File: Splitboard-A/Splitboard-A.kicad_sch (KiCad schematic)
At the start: 111 parts, among them J1 USB_C_Receptacle_USB2.0, J2 USB_C_Receptacle, J3 Conn_01x07, K1 KEYSW, K10 KEYSW, K11 KEYSW, K12 KEYSW, K13 KEYSW, K14 KEYSW, K15 KEYSW, K16 KEYSW, K17 KEYSW, K18 KEYSW, K19 KEYSW, K2 KEYSW, K20 KEYSW, K21 KEYSW, K22 KEYSW, K23 KEYSW, K24 KEYSW, K25 KEYSW, K26 KEYSW, K27 KEYSW, K28 KEYSW, K29 KEYSW, K3 KEYSW, K30 KEYSW, K31 KEYSW, K32 KEYSW, K33 KEYSW, K34 KEYSW, K35 KEYSW, K36 KEYSW, K37 KEYSW, K38 KEYSW, K4 KEYSW, K5 KEYSW, K6 KEYSW, K7 KEYSW, K8 KEYSW, K9 KEYSW, SW1 RotaryEncoder, SW2 SW_Push, U1 AMS1117-3.3, U2 STM32F407VGTx, U3 CR2013-MI2120

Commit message: updated some pins and net labels on sba
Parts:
- C4: value 100nF -> (none)
- C5: value 100nF -> 1uf
- J3: value Conn_01x07 -> (none)
- SW2: value SW_Push -> (none)
- renumbered C1 to C3, C3 to C4, D4 to D1, D13 to D10, D14 to D11, D15 to D12, D16 to D13, D17 to D14, D18 to D15, D19 to D16, D20 to D17, D21 to D18, D22 to D19, D5 to D2, D23 to D20, D24 to D21, D25 to D22, D26 to D23, D27 to D24, D28 to D25, D29 to D26, D30 to D27, D31 to D28, D32 to D29, D6 to D3, D33 to D30, D34 to D31, D35 to D32, D36 to D33, D37 to D34, D38 to D35, D39 to D36, D40 to D37, D41 to D38, D1 to D39, D7 to D4, D2 to D40, D3 to D41, D8 to D5, D9 to D6, D10 to D7, D11 to D8, D12 to D9, J2 to J1, J1 to J2, R3 to R1, R4 to R2, R1 to R3, R2 to R4, U2 to U1, U1 to U2
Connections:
- net +3v3 to micro is gone; now on net +3.3V: C4.1, R3.2, R4.2, U2.2 (VO)
- net Power Regulator is gone; now on net +3.3V: C3.1, D40.2 (A), D41.1 (K), R4.1
- net LCD1_DC: now reaches U1.64 (PC7)
- net LCD1_CS: now reaches U1.65 (PC8)
- net LCD2_DC: now reaches U1.66 (PC9)
- net LCD2_CS: now reaches U1.67 (PA8)
- net LCD2_RESET: now reaches U1.68 (PA9)
- net LCD1_RESET: now reaches U1.69 (PA10)
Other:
- moved on the sheet: U1

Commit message: Updated Schematics with suggestions from course staff
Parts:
- removed C3: 0.1uF, Resistor_SMD:R_0805_2012Metric, symbol Device:C
- removed D40, D41: D_Schottky, Diode_SMD:D_SOD-123, symbol Device:D_Schottky
- removed F1: 500mA, Fuse:Fuse_BelFuse_0ZRE0125FF_L21.2mm_W5.3mm, symbol Device:Fuse
- removed J3: (no value), symbol Connector_Generic:Conn_01x07
- removed R3: 10K, Resistor_SMD:R_0805_2012Metric, symbol Device:R
- added C1, C2: 2u2, Capacitor_SMD:C_0805_2012Metric, symbol Device:C
- added C16, C17: .01uF, Capacitor_SMD:C_0805_2012Metric, symbol Device:C
- added C5, C? (x2): 100nF, Capacitor_SMD:C_0805_2012Metric, symbol Device:C
- added C?: 10uf, Capacitor_SMD:C_0805_2012Metric, symbol Device:C
- added D? (x2): D_Schottky, Diode_SMD:D_SOD-123, symbol Device:D_Schottky
- added J3: Conn_01x06, Connector_PinHeader_2.54mm:PinHeader_1x06_P2.54mm_Horizontal, symbol Connector_Generic:Conn_01x06
- added R10, R11, R12, R13, R14, R5, R6, R7, R8, R9: 10k, Resistor_SMD:R_0805_2012Metric, symbol Device:R
- added R15: 10K, Resistor_SMD:R_0805_2012Metric, symbol Device:R
- added R? (x23): 20, Resistor_SMD:R_0805_2012Metric, symbol Device:R
- added R? (x2): 4k7, Resistor_SMD:R_0805_2012Metric, symbol Device:R
- added U1: SIT2024BA-S2-33E-8.000000G, SIT2024BA:SIT2024BA-S2-33E-8.000000G, symbol SIT2024BA:SIT2024BA-S2-33E-8.000000G
- added U5: USBUF02W6, ul_USBUF02W6:USBUF02W6, symbol USBUF02W6:USBUF02W6
- C10: renamed from C9; footprint (none) -> Capacitor_SMD:C_0805_2012Metric
- C11: renamed from C10; footprint (none) -> Capacitor_SMD:C_0805_2012Metric
- C12: renamed from C11; footprint (none) -> Capacitor_SMD:C_0805_2012Metric
- C13: renamed from C12; footprint (none) -> Capacitor_SMD:C_0805_2012Metric
- C14: renamed from C13; footprint (none) -> Capacitor_SMD:C_0805_2012Metric
- C15: renamed from C14; footprint (none) -> Capacitor_SMD:C_0805_2012Metric
- C18: renamed from C4; value (none) -> 100nF; footprint (none) -> Capacitor_SMD:C_0805_2012Metric
- C6: renamed from C5; value 1uf -> 10uf; footprint (none) -> Capacitor_SMD:C_0805_2012Metric
- C7: renamed from C6; footprint (none) -> Capacitor_SMD:C_0805_2012Metric
- C8: renamed from C7; footprint (none) -> Capacitor_SMD:C_0805_2012Metric
- C9: renamed from C8; footprint (none) -> Capacitor_SMD:C_0805_2012Metric
- J1: renamed from J2; footprint USB_C_Receptacle_GCT_USB4085 -> Connector_USB:USB_C_Receptacle_Amphenol_12401548E4-2A
- J2: renamed from J1; footprint USB_C_Receptacle_GCT_USB4085 -> Connector_USB:USB_C_Receptacle_Amphenol_12401548E4-2A
- R1, R2: value R -> 5K1; footprint (none) -> Resistor_SMD:R_0805_2012Metric
- R4: value 100K -> 10k
- SW1: footprint Rotary_Encoder:RotaryEncoder_Alps_EC12E_Vertical_H20mm -> Rotary_Encoder:RotaryEncoder_Alps_EC11E-Switch_Vertical_H20mm
- SW2: value (none) -> SW_Push; footprint (none) -> Button_Switch_THT:SW_PUSH_6mm
- renumbered C2 to C3, U3 to U2, U1 to U3, U2 to U4
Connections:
- net LCD1_RESET is gone; now on net LCD1_RST: U3.69 (PA10)
- net +3.3V: now also U2.8 (LED), U3.21 (VREF+), U3.22 (VDDA), U3.6 (VBAT), C?.1, D?.1 (K), D?.1 (K), R10.2, R11.1, R13.1, R15.1, R5.2, R6.2, R7.2, R8.2, R9.2, R?.2, R?.2, U1.3 (OE/NC), U1.4 (VDD), U5.5 (VDD); no longer C4.1, J2.A4 (VBUS), J2.A9 (VBUS), J2.B4 (VBUS), J2.B9 (VBUS), R1.1, R2.1, R4.1, U2.1 (VCC), U4.2 (VO)
- net ENC_A: now also C16.1, R12.1, R?.2; no longer R1.2, SW1.A, U3.60 (PD13)
- net ENC_B: now also C17.2, R14.2, R?.2; no longer R2.2, SW1.B, U3.61 (PD14)
- net GND: now also R1.2, R2.2, SW1.S2, U3.20 (VSSA), U3.94 (BOOT0), C1.2, C16.2, C17.1, C2.2, C5.1, C?.2, C?.2, C?.2, J3.3 (Pin_3), U1.1 (GND), U5.2 (GND)
- net LCD1_CS: now also U2.3 (~{CS})
- net LCD1_DC: now also U2.5 (D/~{C})
- net LCD2_CS: now also R?.1
- net LCD2_DC: now also R?.1
- net MOSI: now also U3.18 (PC3), R?.1; no longer J2.B11 (RX1+)
- net NRST: now also J3.5 (Pin_5), R15.2
- net SCK: now also U3.52 (PB13), R?.1; no longer J2.A2 (TX1+)
- net SCL: now also R?.1, R?.1; no longer J2.A10 (RX2-)
- net SDA: now also R?.1, R?.1; no longer J2.A11 (RX2+)
- net SWCLK: now also J3.2 (Pin_2)
- net SWDIO: now also J3.4 (Pin_4)
- net SWO: now also J3.6 (Pin_6)
- net col0: now also R9.1, R?.2; no longer U3.88 (PD7)
- net col1: now also R8.1, R?.2; no longer U3.55 (PD8)
- net col2: now also R7.1, R?.2; no longer U3.56 (PD9)
- net col3: now also R6.1, R?.2; no longer U3.57 (PD10)
- net col4: now also R5.1, R?.2; no longer U3.58 (PD11)
- net col5: now also R4.1, R?.2; no longer U3.59 (PD12)
- net row0: now also R?.2; no longer U3.81 (PD0)
- net row1: now also R?.2; no longer U3.82 (PD1)
- net row2: now also R?.2; no longer U3.83 (PD2)
- net row3: now also R?.2; no longer U3.84 (PD3)
- net row4: now also R?.2; no longer U3.85 (PD4)
- net row5: now also R?.2; no longer U3.86 (PD5)
- net row6: now also R?.2; no longer U3.87 (PD6)
- net at J1.A5 (CC1): now also R1.1
- net at J1.B5 (CC2): now also R2.1
- net USB_CONN_D+: now reaches J1.B6 (D+)
- net USB_CONN_D+: now also J1.A6 (D+), U5.1 (D1)
- net USB_CONN_D-: now reaches J1.B7 (D-)
- net USB_CONN_D-: now also J1.A7 (D-), U5.3 (D2)
- net ENC_SW: now reaches SW1.S1
- net ENC_SW: now also C5.2, R10.1, R?.2
- net at D39.1 (K): now also FB1.1
- net RCC_OSC_IN: now reaches U3.12 (PH0)
- net RCC_OSC_IN: now also U1.5 (OUT)
- net RCC_OSC_OUT: now reaches U3.13 (PH1)
- net at U3.49 (VCAP_1): now also C1.1
- net at U3.62 (PD15): now also R?.1
- net at U3.73 (VCAP_2): now also C2.1
- net LCD1_RST: now reaches U2.4 (RESET)
- net at J2.A5 (CC1): now also J2.B5 (CC2), R?.2
- net at J2.A6 (D+): now also J2.B6 (D+), R?.2
- net at J2.A7 (D-): now also J2.B7 (D-), R?.2
- net at J2.A8 (SBU1): now also J2.B8 (SBU2), R?.2
- net at J2.B2 (TX2+): now also J2.A2 (TX1+)
- net at J2.B3 (TX2-): now also J2.A3 (TX1-), R?.2
- net CS: no longer names the net of J2.B10 (RX1-)
- net CS: now also J2.A10 (RX2-), R?.2; no longer U2.3 (~{CS})
- net LCD2_RESET renamed LCD2_RST
- net LCD2_RST: now also R?.1
- net MISO: no longer names the net of U2.9 (MISO)
- net MISO: no longer J2.A3 (TX1-)
- net TRST: no longer names the net of U3.90 (PB4)
- net USB_DM renamed USB_D-
- net USB_D-: now also U5.4 (D3); no longer J1.A7 (D-)
- net USB_DP renamed USB_D+
- net USB_D+: now also U5.6 (D4); no longer J1.A6 (D+)
- net Voltage Regulator Input renamed VBUS
- net VBUS: now also J2.A4 (VBUS), J2.A9 (VBUS), J2.B4 (VBUS), J2.B9 (VBUS), U2.1 (VCC), C?.1, C?.1
- new net: R?.1, U3.61 (PD14)
- new net: R?.1, U3.55 (PD8)
- new net: R?.1, U3.85 (PD4)
- new net: R11.2, R12.2, SW1.A
- new net: R13.2, R14.1, SW1.B
- new net: R?.1, U3.88 (PD7)
- new net: R?.1, U3.60 (PD13)
- new net: R?.1, U3.57 (PD10)
- new net: R?.1, U3.59 (PD12)
- new net: R?.1, U3.84 (PD3)
- new net: R?.1, U3.86 (PD5)
- new net: D?.2 (A), J3.1 (Pin_1)
- new net: R?.1, U3.56 (PD9)
- new net: R?.1, U3.58 (PD11)
- new net: R?.1, U3.81 (PD0)
- new net: R?.1, U3.82 (PD1)
- new net: R?.1, U3.83 (PD2)
- new net: R?.1, U3.87 (PD6)
- new net: C4.1, D?.2 (A), U4.2 (VO)
- new net: J2.A11 (RX2+), J2.B11 (RX1+), R?.2
- no-connect marks 10 -> 59
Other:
- note added: "10K pullup resistors in case internal don't work These may also end up being 1k"
- note added: "8MHz Oscillator"
- note added: "Does this need decoupling caps?"
- note added: "I have no clue what this circuitry should look like"
- note added: "Likely N/C Add debugging via"
- note added: "Pooling Caps"
- note added: "Put diode in series"
- note added: "SWO: Serial Wire Output"
- note added: "There is an embedded pull up on D+ (for device speed selection)"
- moved on the sheet: C13, C18, C3, C4, C9, D1, D10, D11, D12, D13, D14, D15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

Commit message: Layout changes
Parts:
- gave numbers to parts that had none: 30

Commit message: Layout changes
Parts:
- D39, D40, D41: footprint Diode_SMD:D_SOD-123 -> Diode_SMD:D_SOD-323
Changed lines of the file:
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@@
     (property "Reference" "D39" (id 0) (at 77.7875 260.35 0))
     (property "Value" "D_Schottky" (id 1) (at 77.7875 262.89 0))
-    (property "Footprint" "Diode_SMD:D_SOD-123" (id 2) (at 77.47 266.7 0)
+    (property "Footprint" "Diode_SMD:D_SOD-323" (id 2) (at 77.47 266.7 0)
       (effects (font (size 1.27 1.27)) hide)
     )
@@
     (property "Reference" "D41" (id 0) (at 338.7725 322.58 0))
     (property "Value" "D_Schottky" (id 1) (at 338.7725 325.12 0))
-    (property "Footprint" "Diode_SMD:D_SOD-123" (id 2) (at 339.09 328.93 0)
+    (property "Footprint" "Diode_SMD:D_SOD-323" (id 2) (at 339.09 328.93 0)
       (effects (font (size 1.27 1.27)) hide)
     )
@@
       (effects (font (size 1.27 1.27)) (justify left))
     )
-    (property "Footprint" "Diode_SMD:D_SOD-123" (id 2) (at 121.92 260.35 0)
+    (property "Footprint" "Diode_SMD:D_SOD-323" (id 2) (at 121.92 260.35 0)
       (effects (font (size 1.27 1.27)) hide)
     )
@@
     )
     (path "/5ef3210e-de8e-444d-b7a3-c6a85e5c3868"
-      (reference "D39") (unit 1) (value "D_Schottky") (footprint "Diode_SMD:D_SOD-123")
+      (reference "D39") (unit 1) (value "D_Schottky") (footprint "Diode_SMD:D_SOD-323")
     )
     (path "/f739874a-498f-4d96-a0d9-129228bcf5ee"
-      (reference "D40") (unit 1) (value "D_Schottky") (footprint "Diode_SMD:D_SOD-123")
+      (reference "D40") (unit 1) (value "D_Schottky") (footprint "Diode_SMD:D_SOD-323")
     )
     (path "/cddbd041-5659-459c-b344-e0c4b795f57d"
-      (reference "D41") (unit 1) (value "D_Schottky") (footprint "Diode_SMD:D_SOD-123")
+      (reference "D41") (unit 1) (value "D_Schottky") (footprint "Diode_SMD:D_SOD-323")
     )
     (path "/f3cc7ab8-c40c-45a6-9789-37cfaf8bc1a0"

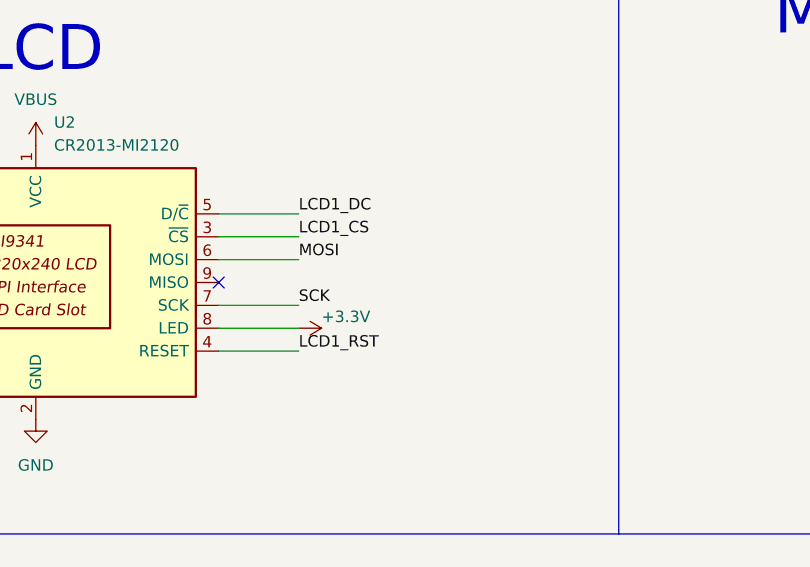
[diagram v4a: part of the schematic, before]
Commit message: Addes rseries for LCD and added extra vias
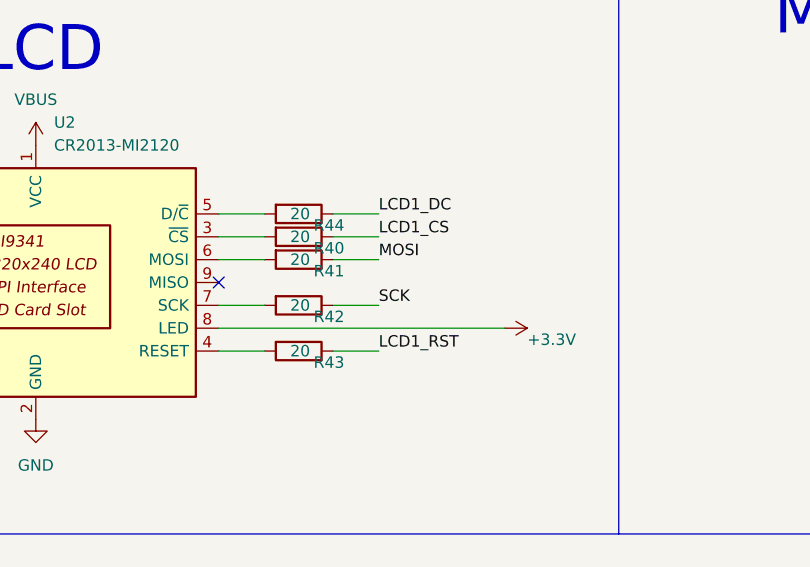
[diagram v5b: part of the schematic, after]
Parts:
- added R40, R41, R42, R43, R44: 20, Resistor_SMD:R_0805_2012Metric, symbol Device:R
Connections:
- net LCD1_CS: now also R40.1; no longer U2.3 (~{CS})
- net LCD1_DC: now also R44.1; no longer U2.5 (D/~{C})
- net LCD1_RST: now also R43.1; no longer U2.4 (RESET)
- net MOSI: now also R41.1; no longer U2.6 (MOSI)
- net SCK: now also R42.1; no longer U2.7 (SCK)
- new net: R41.2, U2.6 (MOSI)
- new net: R43.2, U2.4 (RESET)
- new net: R44.2, U2.5 (D/~{C})
- new net: R40.2, U2.3 (~{CS})
- new net: R42.2, U2.7 (SCK)
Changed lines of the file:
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@@
     (stroke (width 0) (type default) (color 0 0 0 0))
   )
-  (wire (pts (xy 441.96 73.66) (xy 450.85 73.66))
+  (wire (pts (xy 441.96 73.66) (xy 447.04 73.66))
     (stroke (width 0) (type default) (color 0 0 0 0))
   )
@@
     (stroke (width 0) (type default) (color 0 0 0 0))
   )
+  (wire (pts (xy 454.66 58.42) (xy 459.74 58.42))
+    (stroke (width 0) (type default) (color 0 0 0 0))
+  )
   (wire (pts (xy 444.5 363.22) (xy 455.93 363.22))
     (stroke (width 0) (type default) (color 0 0 0 0))
@@
     (stroke (width 0) (type default) (color 0 0 0 0))
   )
-  (wire (pts (xy 450.85 60.96) (xy 441.96 60.96))
+  (wire (pts (xy 459.74 60.96) (xy 454.66 60.96))
     (stroke (width 0) (type default) (color 0 0 0 0))
   )
@@
     (stroke (width 0) (type default) (color 0 0 0 0))
   )
-  (wire (pts (xy 450.85 68.58) (xy 441.96 68.58))
+  (wire (pts (xy 459.74 68.58) (xy 454.66 68.58))
     (stroke (width 0) (type default) (color 0 0 0 0))
   )
@@
     (stroke (width 0) (type default) (color 0 0 0 0))
   )
-  (wire (pts (xy 441.96 71.12) (xy 450.85 71.12))
+  (wire (pts (xy 441.96 71.12) (xy 473.71 71.12))
     (stroke (width 0) (type default) (color 0 0 0 0))
   )
@@
     (stroke (width 0) (type default) (color 0 0 0 0))
   )
+  (wire (pts (xy 454.66 73.66) (xy 459.74 73.66))
+    (stroke (width 0) (type default) (color 0 0 0 0))
+  )
   (wire (pts (xy 87.63 49.53) (xy 93.98 49.53))
     (stroke (width 0) (type default) (color 0 0 0 0))
@@
     (stroke (width 0) (type default) (color 0 0 0 0))
   )
-  (wire (pts (xy 441.96 58.42) (xy 450.85 58.42))
+  (wire (pts (xy 441.96 58.42) (xy 447.04 58.42))
     (stroke (width 0) (type default) (color 0 0 0 0))
   )
@@
     (stroke (width 0) (type default) (color 0 0 0 0))
   )
+  (wire (pts (xy 447.04 63.5) (xy 441.96 63.5))
+    (stroke (width 0) (type default) (color 0 0 0 0))
+  )
   (wire (pts (xy 420.37 167.64) (xy 419.1 167.64))
     (stroke (width 0) (type default) (color 0 0 0 0))
@@
     (stroke (width 0) (type default) (color 0 0 0 0))
   )
+  (wire (pts (xy 447.04 60.96) (xy 441.96 60.96))
+    (stroke (width 0) (type default) (color 0 0 0 0))
+  )
   (wire (pts (xy 485.14 176.53) (xy 485.14 177.8))
     (stroke (width 0) (type default) (color 0 0 0 0))
@@
     (stroke (width 0) (type default) (color 0 0 0 0))
   )
-  (wire (pts (xy 450.85 63.5) (xy 441.96 63.5))
+  (wire (pts (xy 459.74 63.5) (xy 454.66 63.5))
     (stroke (width 0) (type default) (color 0 0 0 0))
   )
@@
     (stroke (width 0) (type default) (color 0 0 0 0))
   )
+  (wire (pts (xy 447.04 68.58) (xy 441.96 68.58))
+    (stroke (width 0) (type default) (color 0 0 0 0))
+  )
   (wire (pts (xy 530.86 167.64) (xy 529.59 167.64))
     (stroke (width 0) (type default) (color 0 0 0 0))
@@
     (effects (font (size 1.27 1.27)) (justify left bottom))
   )
-  (label "LCD1_CS" (at 450.85 60.96 0)
+  (label "LCD1_CS" (at 459.74 60.96 0)
     (effects (font (size 1.27 1.27)) (justify left bottom))
   )
@@
     (effects (font (size 1.27 1.27)) (justify left bottom))
   )
-  (label "SCK" (at 450.85 68.58 0)
+  (label "SCK" (at 459.74 68.58 0)
     (effects (font (size 1.27 1.27)) (justify left bottom))
   )
@@
     (effects (font (size 1.27 1.27)) (justify left bottom))
   )
-  (label "LCD1_RST" (at 450.85 73.66 0)
+  (label "LCD1_RST" (at 459.74 73.66 0)
     (effects (font (size 1.27 1.27)) (justify left bottom))
   )
@@
     (effects (font (size 1.27 1.27)) (justify left bottom))
   )
-  (label "MOSI" (at 450.85 63.5 0)
+  (label "MOSI" (at 459.74 63.5 0)
     (effects (font (size 1.27 1.27)) (justify left bottom))
   )
@@
     (effects (font (size 1.27 1.27)) (justify left bottom))
   )
-  (label "LCD1_DC" (at 450.85 58.42 0)
+  (label "LCD1_DC" (at 459.74 58.42 0)
     (effects (font (size 1.27 1.27)) (justify left bottom))
   )
@@
     (pin "1")
   )
-  (symbol (lib_id "power:+3.3V") (at 450.85 71.12 270) (unit 1)
+  (symbol (lib_id "power:+3.3V") (at 473.71 71.12 270) (unit 1)
     (in_bom yes) (on_board yes)
-    (property "Reference" "#PWR06" (id 0) (at 447.04 71.12 0)
+    (property "Reference" "#PWR06" (id 0) (at 469.9 71.12 0)
       (effects (font (size 1.27 1.27)) hide)
     )
-    (property "Value" "+3.3V" (id 1) (at 453.39 69.85 90)
+    (property "Value" "+3.3V" (id 1) (at 476.25 72.39 90)
       (effects (font (size 1.27 1.27)) (justify left))
     )
-    (property "Footprint" "" (id 2) (at 450.85 71.12 0)
+    (property "Footprint" "" (id 2) (at 473.71 71.12 0)
       (effects (font (size 1.27 1.27)) hide)
     )
-    (property "Datasheet" "" (id 3) (at 450.85 71.12 0)
+    (property "Datasheet" "" (id 3) (at 473.71 71.12 0)
       (effects (font (size 1.27 1.27)) hide)
     )
@@
     (pin "2")
   )
+  (symbol (lib_id "Device:R") (at 450.85 63.5 270) (unit 1)
+    (in_bom yes) (on_board yes)
+    (property "Reference" "R41" (id 0) (at 455.93 64.77 90)
+      (effects (font (size 1.27 1.27)) (justify right))
+    )
+    (property "Value" "20" (id 1) (at 452.12 63.5 90)
+      (effects (font (size 1.27 1.27)) (justify right))
+    )
+    (property "Footprint" "Resistor_SMD:R_0805_2012Metric" (id 2) (at 450.85 61.722 90)
+      (effects (font (size 1.27 1.27)) hide)
+    )
+    (property "Datasheet" "~" (id 3) (at 450.85 63.5 0)
+      (effects (font (size 1.27 1.27)) hide)
+    )
+    (pin "1")
+    (pin "2")
+  )
   (symbol (lib_id "power:GND") (at 110.49 278.13 0) (unit 1)
     (in_bom yes) (on_board yes) (fields_autoplaced)
@@
     (pin "2")
   )
+  (symbol (lib_id "Device:R") (at 450.85 73.66 270) (unit 1)
+    (in_bom yes) (on_board yes)
+    (property "Reference" "R43" (id 0) (at 455.93 74.93 90)
+      (effects (font (size 1.27 1.27)) (justify right))
+    )
+    (property "Value" "20" (id 1) (at 452.12 73.66 90)
+      (effects (font (size 1.27 1.27)) (justify right))
+    )
+    (property "Footprint" "Resistor_SMD:R_0805_2012Metric" (id 2) (at 450.85 71.882 90)
+      (effects (font (size 1.27 1.27)) hide)
+    )
+    (property "Datasheet" "~" (id 3) (at 450.85 73.66 0)
+      (effects (font (size 1.27 1.27)) hide)
+    )
+    (pin "1")
+    (pin "2")
+  )
   (symbol (lib_id "Device:C") (at 506.73 359.41 0) (unit 1)
     (in_bom yes) (on_board yes) (fields_autoplaced)
@@
     (pin "2")
   )
+  (symbol (lib_id "Device:R") (at 450.85 58.42 270) (unit 1)
+    (in_bom yes) (on_board yes)
+    (property "Reference" "R44" (id 0) (at 455.93 59.69 90)
+      (effects (font (size 1.27 1.27)) (justify right))
+    )
+    (property "Value" "20" (id 1) (at 452.12 58.42 90)
+      (effects (font (size 1.27 1.27)) (justify right))
+    )
+    (property "Footprint" "Resistor_SMD:R_0805_2012Metric" (id 2) (at 450.85 56.642 90)
+      (effects (font (size 1.27 1.27)) hide)
+    )
+    (property "Datasheet" "~" (id 3) (at 450.85 58.42 0)
+      (effects (font (size 1.27 1.27)) hide)
+    )
+    (pin "1")
+    (pin "2")
+  )
   (symbol (lib_id "Device:R") (at 218.44 372.11 270) (unit 1)
     (in_bom yes) (on_board yes) (fields_autoplaced)
@@
     (pin "2")
   )
+  (symbol (lib_id "Device:R") (at 450.85 60.96 270) (unit 1)
+    (in_bom yes) (on_board yes)
+    (property "Reference" "R40" (id 0) (at 455.93 62.23 90)
+      (effects (font (size 1.27 1.27)) (justify right))
+    )
+    (property "Value" "20" (id 1) (at 452.12 60.96 90)
+      (effects (font (size 1.27 1.27)) (justify right))
+    )
+    (property "Footprint" "Resistor_SMD:R_0805_2012Metric" (id 2) (at 450.85 59.182 90)
+      (effects (font (size 1.27 1.27)) hide)
+    )
+    (property "Datasheet" "~" (id 3) (at 450.85 60.96 0)
+      (effects (font (size 1.27 1.27)) hide)
+    )
+    (pin "1")
+    (pin "2")
+  )
   (symbol (lib_id "Regulator_Linear:AMS1117-3.3") (at 110.49 266.7 0) (unit 1)
     (in_bom yes) (on_board yes) (fields_autoplaced)
@@
     (pin "2")
   )
+  (symbol (lib_id "Device:R") (at 450.85 68.58 270) (unit 1)
+    (in_bom yes) (on_board yes)
+    (property "Reference" "R42" (id 0) (at 455.93 69.85 90)
+      (effects (font (size 1.27 1.27)) (justify right))
+    )
+    (property "Value" "20" (id 1) (at 452.12 68.58 90)
+      (effects (font (size 1.27 1.27)) (justify right))
+    )
+    (property "Footprint" "Resistor_SMD:R_0805_2012Metric" (id 2) (at 450.85 66.802 90)
+      (effects (font (size 1.27 1.27)) hide)
+    )
+    (property "Datasheet" "~" (id 3) (at 450.85 68.58 0)
+      (effects (font (size 1.27 1.27)) hide)
+    )
+    (pin "1")
+    (pin "2")
+  )
   (symbol (lib_id "power:GND") (at 339.09 334.01 0) (unit 1)
     (in_bom yes) (on_board yes)
@@
       (reference "R39") (unit 1) (value "4k7") (footprint "Resistor_SMD:R_0805_2012Metric")
     )
+    (path "/9b265d64-12fe-42b7-8f50-f1bf80e1a3de"
+      (reference "R40") (unit 1) (value "20") (footprint "Resistor_SMD:R_0805_2012Metric")
+    )
+    (path "/1074d397-b4ca-4669-a8cb-fcc564b50cdd"
+      (reference "R41") (unit 1) (value "20") (footprint "Resistor_SMD:R_0805_2012Metric")
+    )
+    (path "/da664f50-d9d5-4f2d-a094-48d110c18179"
+      (reference "R42") (unit 1) (value "20") (footprint "Resistor_SMD:R_0805_2012Metric")
+    )
+    (path "/4c8bbfbf-d048-4e56-96f7-69d184a219ce"
+      (reference "R43") (unit 1) (value "20") (footprint "Resistor_SMD:R_0805_2012Metric")
+    )
+    (path "/8bd2d1bb-52df-4de7-96de-0b3da3df2790"
+      (reference "R44") (unit 1) (value "20") (footprint "Resistor_SMD:R_0805_2012Metric")
+    )
     (path "/38fe4bc3-8fec-480e-9eda-33bcbef5df4c"
